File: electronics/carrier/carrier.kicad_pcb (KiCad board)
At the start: 2 copper layers, 100 x 70 mm, 15 parts, among them J1 5 V barrel input (fitted in r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, J2 USB-C power input, PD (laid o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, J3 S3 USB: link to the P4 and fl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, J4 5 V out to the P4 board's USB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, J5 HUB75 ribbon to the LED panel, J6 5 V power to the LED panel, J7 INMP441 microphone cable, J8 Future serial link to the P4'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, SW1 S3 reset, SW2 S3 boot, U1 ESP32-S3-WROOM-1-N16R8

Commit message: Add the carrier board schematic, generated from one netlist
tools/netlist.py describes every part and pin net; gen_schematic.py writes
the KiCad schematic from it and build_board.py puts every pad on its net, so
the schematic and board cannot disagree (KiCad parity check: 0 differences;
ERC clean apart from three intentional input ties).

Circuit: barrel 5 V input with polyfuse, TVS and bulk capacitance; USB-C PD
path laid out but not fitted (CH224A requesting 15 V, TPS568215 to 5 V with
TI's datasheet values) selected by solder jumper; AP2112K 3.3 V;
ESP32-S3-WROOM-1 with reset/boot, USB-C with ESD protection and 5.1k CC
resistors; two 74AHCT245 buffers to a standard HUB75 socket on the firmware's
existing GPIOs; microphone, fused P4 power and future UART connectors.

Co-Authored-By: Claude Opus 5.5 <noreply@anthropic.com>
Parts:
- added C1: 1000uF 10V, Capacitor_SMD:CP_Elec_10x10.5, F.Cu at (195.0, 82.0)
- added C10: 1uF 25V, Capacitor_SMD:C_0805_2012Metric, F.Cu at (217.0, 73.0)
- added C11: 100nF, Capacitor_SMD:C_0603_1608Metric, F.Cu at (217.0, 91.0)
- added C12: 150pF, Capacitor_SMD:C_0603_1608Metric, F.Cu at (217.0, 127.0)
- added C13: 4.7uF, Capacitor_SMD:C_0805_2012Metric, F.Cu at (217.0, 154.0)
- added C14: 10uF 25V, Capacitor_SMD:C_1206_3216Metric, F.Cu at (217.0, 181.0)
- added C15: 10uF 25V, Capacitor_SMD:C_1206_3216Metric, F.Cu at (217.0, 190.0)
- added C16: 10uF 25V, Capacitor_SMD:C_1206_3216Metric, F.Cu at (217.0, 199.0)
- added C17: 10uF 25V, Capacitor_SMD:C_1206_3216Metric, F.Cu at (217.0, 208.0)
- added C18: 100nF 25V, Capacitor_SMD:C_0603_1608Metric, F.Cu at (217.0, 217.0)
- added C19: 22uF 10V, Capacitor_SMD:C_1206_3216Metric, F.Cu at (217.0, 226.0)
- added C2: 22uF 10V, Capacitor_SMD:C_1206_3216Metric, F.Cu at (195.0, 91.0)
- added C20: 22uF 10V, Capacitor_SMD:C_1206_3216Metric, F.Cu at (217.0, 235.0)
- added C21: 22uF 10V, Capacitor_SMD:C_1206_3216Metric, F.Cu at (217.0, 244.0)
- added C22: 22uF 10V, Capacitor_SMD:C_1206_3216Metric, F.Cu at (217.0, 253.0)
- added C23: 22uF 10V, Capacitor_SMD:C_1206_3216Metric, F.Cu at (217.0, 262.0)
- added C24: 100nF, Capacitor_SMD:C_0603_1608Metric, F.Cu at (283.0, 82.0)
- added C25: 100nF, Capacitor_SMD:C_0603_1608Metric, F.Cu at (283.0, 91.0)
- added C3: 100nF, Capacitor_SMD:C_0603_1608Metric, F.Cu at (195.0, 100.0)
- added C4: 1uF, Capacitor_SMD:C_0603_1608Metric, F.Cu at (261.0, 64.0)
- added C5: 22uF, Capacitor_SMD:C_1206_3216Metric, F.Cu at (261.0, 82.0)
- added C6: 100nF, Capacitor_SMD:C_0603_1608Metric, F.Cu at (261.0, 91.0)
- added C7: 1uF, Capacitor_SMD:C_0603_1608Metric, F.Cu at (239.0, 64.0)
- added C8: 1uF, Capacitor_SMD:C_0603_1608Metric, F.Cu at (239.0, 73.0)
- added D1: SMAJ5.0A, Diode_SMD:D_SMA, F.Cu at (195.0, 73.0)
- added D2: Green, LED_SMD:LED_0603_1608Metric, F.Cu at (239.0, 82.0)
- added F1: 6A hold, Fuse:Fuse_2920_7451Metric, F.Cu at (195.0, 55.0)
- added F2: 2.5A hold, Fuse:Fuse_1812_4532Metric, F.Cu at (305.0, 55.0)
- added JP1: Barrel input, Jumper:SolderJumper-2_P1.3mm_Bridged_RoundedPad1.0x1.5mm, F.Cu at (195.0, 64.0)
- added JP2: USB-C input, Jumper:SolderJumper-2_P1.3mm_Open_RoundedPad1.0x1.5mm, F.Cu at (217.0, 271.0)
- added L1: 2.2uH 10A, Inductor_SMD:L_Coilcraft_XAL7070-XXX, F.Cu at (217.0, 100.0)
- added R1: 10k, Resistor_SMD:R_0603_1608Metric, F.Cu at (261.0, 55.0)
- added R10: 56k, Resistor_SMD:R_0603_1608Metric, F.Cu at (217.0, 64.0)
- added R11: 73.2k, Resistor_SMD:R_0603_1608Metric, F.Cu at (217.0, 109.0)
- added R12: 10k, Resistor_SMD:R_0603_1608Metric, F.Cu at (217.0, 118.0)
- added R13: 100k, Resistor_SMD:R_0603_1608Metric, F.Cu at (217.0, 136.0)
- added R14: 10k, Resistor_SMD:R_0603_1608Metric, F.Cu at (217.0, 145.0)
- added R15: 120k, Resistor_SMD:R_0603_1608Metric, F.Cu at (217.0, 163.0)
- added R16: 20k, Resistor_SMD:R_0603_1608Metric, F.Cu at (217.0, 172.0)
- added R2: 10k, Resistor_SMD:R_0603_1608Metric, F.Cu at (261.0, 73.0)
- added R3: 5.1k, Resistor_SMD:R_0603_1608Metric, F.Cu at (261.0, 100.0)
- added R4: 5.1k, Resistor_SMD:R_0603_1608Metric, F.Cu at (261.0, 109.0)
- added R5: 1k, Resistor_SMD:R_0603_1608Metric, F.Cu at (239.0, 91.0)
- added R6: 10k, Resistor_SMD:R_0603_1608Metric, F.Cu at (283.0, 55.0)
- added U2: CH224A, Package_SO:SSOP-10-1EP_3.9x4.9mm_P1mm_EP2.1x3.3mm, F.Cu at (217.0, 55.0)
- added U3: TPS568215, Package_DFN_QFN:Texas_RNN0018A, F.Cu at (217.0, 82.0)
- added U4: USBLC6-2SC6, Package_TO_SOT_SMD:SOT-23-6, F.Cu at (261.0, 118.0)
- added U5: AP2112K-3.3, Package_TO_SOT_SMD:SOT-23-5, F.Cu at (239.0, 55.0)
- added U6: 74AHCT245, Package_SO:TSSOP-20_4.4x6.5mm_P0.65mm, F.Cu at (283.0, 64.0)
- added U7: 74AHCT245, Package_SO:TSSOP-20_4.4x6.5mm_P0.65mm, F.Cu at (283.0, 73.0)
- H1, H2, H3, H4: value M3 to heat-set insert -> M3; footprint MountingHole_3.2mm_M3 -> MountingHole:MountingHole_3.2mm_M3
- J1: value 5 V barrel input (fitted in revision 1) -> PJ-063AH; footprint BarrelJack_CUI_PJ-063AH_Horizontal -> Connector_BarrelJack:BarrelJack_CUI_PJ-063AH_Horizontal
- J2: value USB-C power input, PD (laid out, fitted later) -> USB-C power in; footprint USB_C_Receptacle_HRO_TYPE-C-31-M-12 -> Connector_USB:USB_C_Receptacle_HRO_TYPE-C-31-M-12
- J3: value S3 USB: link to the P4 and flashing -> S3 USB (P4 link, flashing); footprint USB_C_Receptacle_GCT_USB4105-xx-A_16P_TopMnt_Horizontal -> Connector_USB:USB_C_Receptacle_GCT_USB4105-xx-A_16P_TopMnt_Horizontal
- J4: value 5 V out to the P4 board's USB-C -> 5V to P4; footprint USB_A_Molex_67643_Horizontal -> Connector_USB:USB_A_Molex_67643_Horizontal
- J5: value HUB75 ribbon to the LED panel -> HUB75; footprint IDC-Header_2x08_P2.54mm_Vertical -> Connector_IDC:IDC-Header_2x08_P2.54mm_Vertical
- J6: value 5 V power to the LED panel -> LED panel 5V; footprint TerminalBlock_Phoenix_MKDS-1,5-2-5.08_1x02_P5.08mm_Horizontal -> TerminalBlock_Phoenix:TerminalBlock_Phoenix_MKDS-1,5-2-5.08_1x02_P5.08mm_Horizontal
- J7: value INMP441 microphone cable -> INMP441; footprint JST_PH_B6B-PH-K_1x06_P2.00mm_Vertical -> Connector_JST:JST_PH_B6B-PH-K_1x06_P2.00mm_Vertical
- J8: value Future serial link to the P4's UART socket (not fitted) -> P4 UART (future); footprint JST_PH_B4B-PH-K_1x04_P2.00mm_Vertical -> Connector_JST:JST_PH_B4B-PH-K_1x04_P2.00mm_Vertical
- SW1: value S3 reset -> Reset; footprint SW_SPST_TL3342 -> Button_Switch_SMD:SW_SPST_TL3342
- SW2: value S3 boot -> Boot; footprint SW_SPST_TL3342 -> Button_Switch_SMD:SW_SPST_TL3342
- U1: footprint ESP32-S3-WROOM-1 -> RF_Module:ESP32-S3-WROOM-1
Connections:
- J1 pad 1: (no net) -> /VIN_BARREL
- J1 pad 2: (no net) -> /GND
- J2 pad A1: (no net) -> /GND
- J2 pad A12: (no net) -> /GND
- J2 pad A4: (no net) -> /VBUS_PD
- J2 pad A5: (no net) -> /PD_CC1
- J2 pad A6: (no net) -> unconnected-(J2-D+-PadA6)
- J2 pad A7: (no net) -> unconnected-(J2-D--PadA7)
- J2 pad A8: (no net) -> unconnected-(J2-SBU1-PadA8)
- J2 pad A9: (no net) -> /VBUS_PD
- J2 pad B1: (no net) -> /GND
- J2 pad B12: (no net) -> /GND
- J2 pad B4: (no net) -> /VBUS_PD
- J2 pad B5: (no net) -> /PD_CC2
- J2 pad B6: (no net) -> unconnected-(J2-D+-PadB6)
- J2 pad B7: (no net) -> unconnected-(J2-D--PadB7)
- J2 pad B8: (no net) -> unconnected-(J2-SBU2-PadB8)
- J2 pad B9: (no net) -> /VBUS_PD
- J2 pad SH: (no net) -> /GND
- J3 pad A1: (no net) -> /GND
- J3 pad A12: (no net) -> /GND
- J3 pad A4: (no net) -> /S3_VBUS
- J3 pad A5: (no net) -> /S3_CC1
- J3 pad A6: (no net) -> /USB_DP
- J3 pad A7: (no net) -> /USB_DM
- J3 pad A8: (no net) -> unconnected-(J3-SBU1-PadA8)
- J3 pad A9: (no net) -> /S3_VBUS
- J3 pad B1: (no net) -> /GND
- J3 pad B12: (no net) -> /GND
- J3 pad B4: (no net) -> /S3_VBUS
- J3 pad B5: (no net) -> /S3_CC2
- J3 pad B6: (no net) -> /USB_DP
- J3 pad B7: (no net) -> /USB_DM
- J3 pad B8: (no net) -> unconnected-(J3-SBU2-PadB8)
- J3 pad B9: (no net) -> /S3_VBUS
- J3 pad SH: (no net) -> /GND
- J4 pad 1: (no net) -> /P4_5V
- J4 pad 2: (no net) -> unconnected-(J4-D--Pad2)
- J4 pad 3: (no net) -> unconnected-(J4-D+-Pad3)
- J4 pad 4: (no net) -> /GND
- J4 pad SH: (no net) -> /GND
- J5 pad 1: (no net) -> /HUB_R1
- J5 pad 10: (no net) -> /HUB_B
- J5 pad 11: (no net) -> /HUB_C
- J5 pad 12: (no net) -> /HUB_D
- J5 pad 13: (no net) -> /HUB_CLK
- J5 pad 14: (no net) -> /HUB_LAT
- J5 pad 15: (no net) -> /HUB_OE
- J5 pad 16: (no net) -> /GND
- J5 pad 2: (no net) -> /HUB_G1
- J5 pad 3: (no net) -> /HUB_B1
- J5 pad 4: (no net) -> /GND
- J5 pad 5: (no net) -> /HUB_R2
- J5 pad 6: (no net) -> /HUB_G2
- J5 pad 7: (no net) -> /HUB_B2
- J5 pad 8: (no net) -> /GND
- J5 pad 9: (no net) -> /HUB_A
- J6 pad 1: (no net) -> /+5V
- J6 pad 2: (no net) -> /GND
- J7 pad 1: (no net) -> /+3V3
- J7 pad 2: (no net) -> /GND
- J7 pad 3: (no net) -> /MIC_SCK
- J7 pad 4: (no net) -> /MIC_WS
- J7 pad 5: (no net) -> /MIC_SD
- J7 pad 6: (no net) -> /GND
- J8 pad 1: (no net) -> /GND
- J8 pad 2: (no net) -> /S3_UART_TX
- J8 pad 3: (no net) -> /S3_UART_RX
- J8 pad 4: (no net) -> unconnected-(J8-Pin_4-Pad4)
- SW1 pad 1: (no net) -> /S3_EN
- SW1 pad 2: (no net) -> /GND
- SW2 pad 1: (no net) -> /S3_BOOT
- SW2 pad 2: (no net) -> /GND
- U1 pad 1: (no net) -> /GND
- U1 pad 10: (no net) -> /S3_CLK
- U1 pad 11: (no net) -> /S3_LAT
- U1 pad 12: (no net) -> /S3_G1
- U1 pad 13: (no net) -> /USB_DM
- U1 pad 14: (no net) -> /USB_DP
- U1 pad 15: (no net) -> unconnected-(U1-IO3-Pad15)
- U1 pad 16: (no net) -> unconnected-(U1-IO46-Pad16)
- U1 pad 17: (no net) -> /S3_B1
- U1 pad 18: (no net) -> /S3_R2
- U1 pad 19: (no net) -> /S3_G2
- U1 pad 2: (no net) -> /+3V3
- U1 pad 20: (no net) -> /S3_B2
- U1 pad 21: (no net) -> /S3_A
- U1 pad 22: (no net) -> /S3_B
- U1 pad 23: (no net) -> /S3_OE
- U1 pad 24: (no net) -> unconnected-(U1-IO47-Pad24)
- U1 pad 25: (no net) -> unconnected-(U1-IO48-Pad25)
- U1 pad 26: (no net) -> unconnected-(U1-IO45-Pad26)
- U1 pad 27: (no net) -> /S3_BOOT
- U1 pad 28: (no net) -> unconnected-(U1-IO35-Pad28)
- U1 pad 29: (no net) -> unconnected-(U1-IO36-Pad29)
- U1 pad 3: (no net) -> /S3_EN
- U1 pad 30: (no net) -> unconnected-(U1-IO37-Pad30)
- U1 pad 31: (no net) -> unconnected-(U1-IO38-Pad31)
- U1 pad 32: (no net) -> unconnected-(U1-IO39-Pad32)
- U1 pad 33: (no net) -> unconnected-(U1-IO40-Pad33)
- U1 pad 34: (no net) -> unconnected-(U1-IO41-Pad34)
- U1 pad 35: (no net) -> unconnected-(U1-IO42-Pad35)
- U1 pad 36: (no net) -> unconnected-(U1-RXD0-Pad36)
- U1 pad 37: (no net) -> unconnected-(U1-TXD0-Pad37)
- U1 pad 38: (no net) -> /S3_UART_RX
- U1 pad 39: (no net) -> /S3_UART_TX
- U1 pad 4: (no net) -> /S3_R1
- U1 pad 40: (no net) -> /GND
- U1 pad 41: (no net) -> /GND
- U1 pad 5: (no net) -> /MIC_SCK
- U1 pad 6: (no net) -> /MIC_WS
- U1 pad 7: (no net) -> /MIC_SD
- U1 pad 8: (no net) -> /S3_C
- U1 pad 9: (no net) -> /S3_D

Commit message: Place every carrier board part
Power-input protection under the barrel socket; the USB-C power section
grouped at the rear middle by its socket; the 3.3 V supply and decoupling
beside the module; ESD and CC resistors at the S3's USB-C; the buffers
between the module and the HUB75 socket; buttons and the power LED on the
front strip. Nothing in the module's antenna keep-out; schematic parity 0.

Co-Authored-By: Claude Opus 5.5 <noreply@anthropic.com>
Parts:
- moved F2 238.2 mm to (70.0, 94.0), turned to 90 degrees
- moved JP2 215.3 mm to (118.5, 79.5)
- moved C23 211.1 mm to (118.0, 75.5)
- moved C22 203.6 mm to (113.0, 78.0)
- moved U4 201.9 mm to (64.0, 74.0), turned to 90 degrees
- moved R3 201.3 mm to (62.0, 69.5)
- moved R4 201.2 mm to (62.0, 79.0)
- moved C21 198.0 mm to (113.0, 75.5)
- moved C20 191.1 mm to (108.0, 78.0)
- moved U6 190.7 mm to (94.0, 89.5), turned to 90 degrees
- moved C24 189.0 mm to (94.0, 83.5)
- moved C18 186.0 mm to (100.5, 72.0), turned to 90 degrees
- moved C19 185.8 mm to (108.0, 75.5)
- moved C17 185.0 mm to (91.0, 72.5), turned to 90 degrees
- moved R2 181.7 mm to (83.5, 112.0), turned to 90 degrees
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
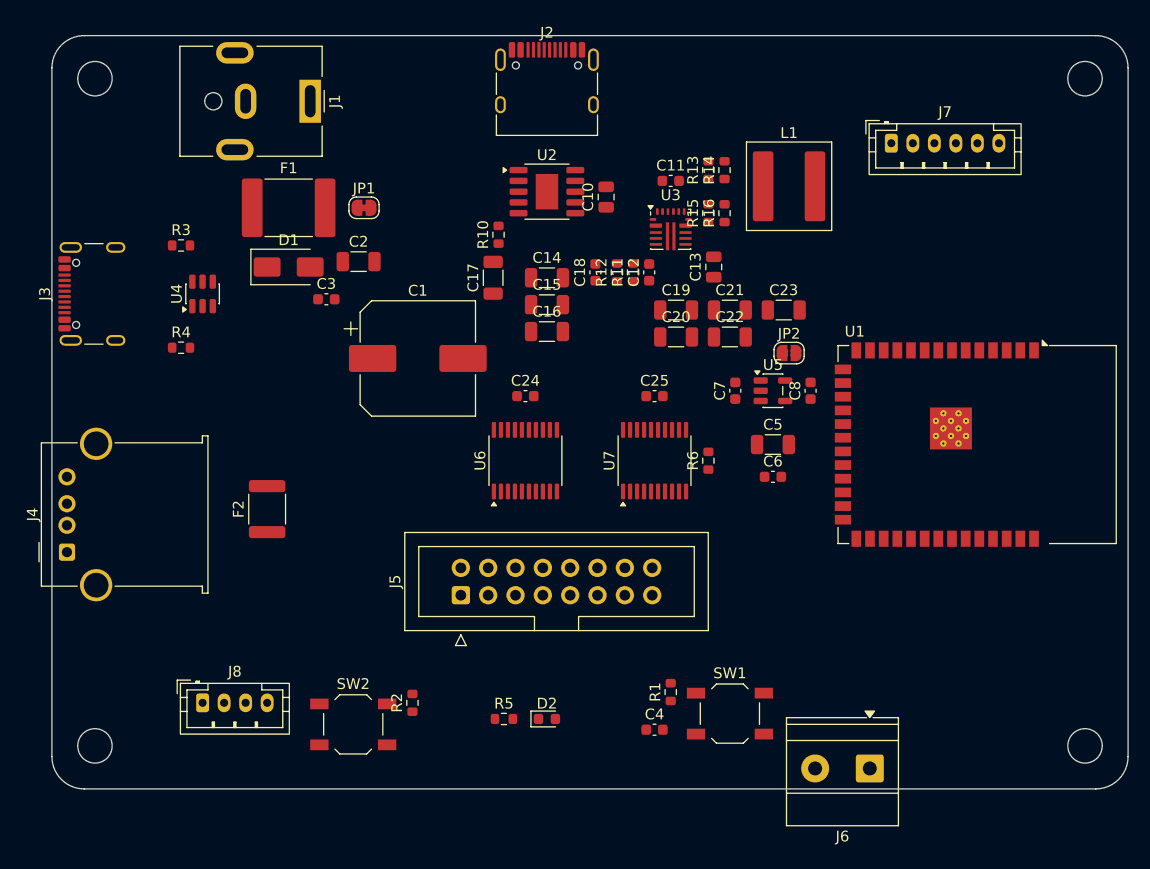
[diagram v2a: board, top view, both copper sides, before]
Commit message: Route the carrier board
Add route_board.py: locked high-current and fine-pitch copper, Freerouting
for the rest, ground pours and stitching vias, then KiCad's own check for
anything left unconnected. The board passes DRC with no errors, nothing
unconnected and exact schematic parity.

- Remove the solder jumpers: F1 alone selects the barrel input, and the
  USB-C buck output feeds +5V directly.
- Name stacked unconnected pins as KiCad does, so the S3 socket's paired
  VBUS pads share one net.
- Rotate U3 so its switch node runs straight to L1; move the MODE/EN
  dividers and the boot capacitor to suit. Swap R3/R4 to match their CC pins.
- Hide chip passive references on the silkscreen; allow ref positions in
  board.json; allow one thermal spoke on through-hole pads (.kicad_dru).

Co-Authored-By: Claude Opus 5.5 <noreply@anthropic.com>
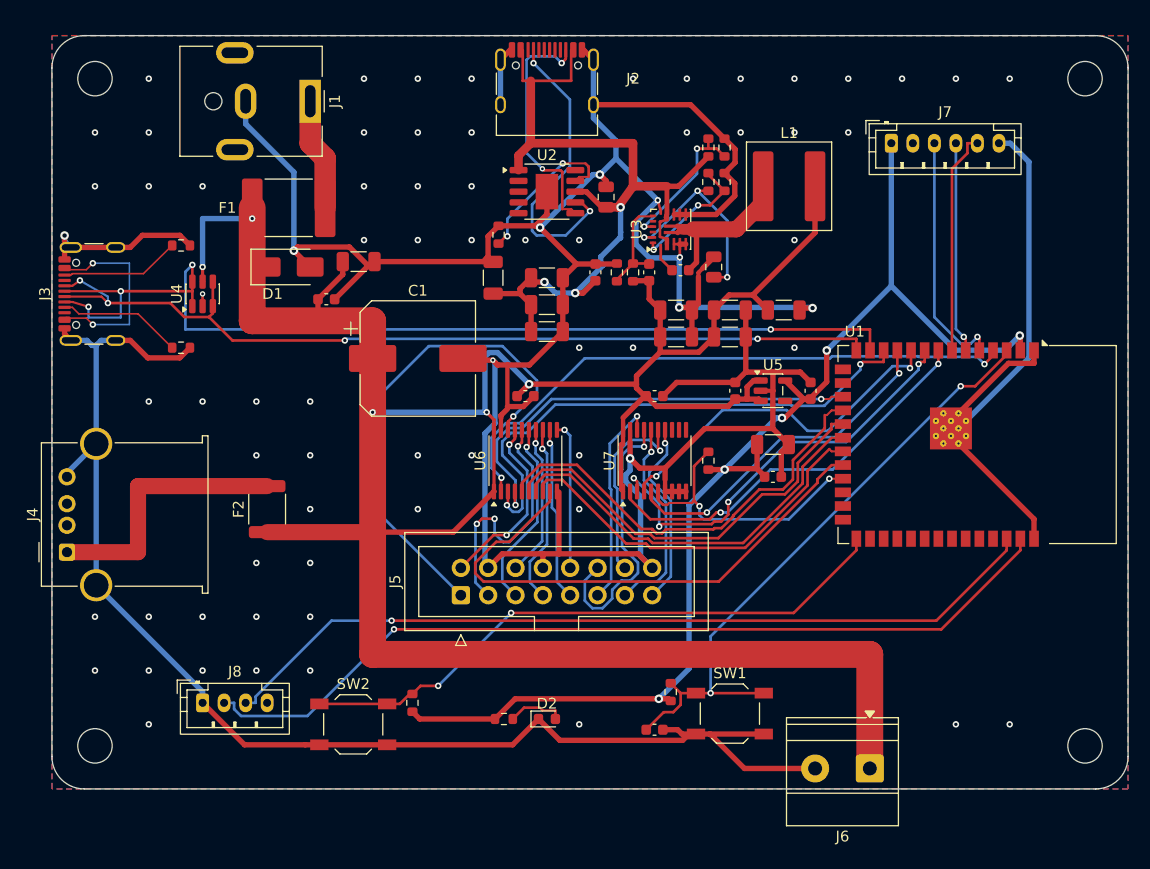
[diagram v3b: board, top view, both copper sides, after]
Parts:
- removed JP1: Barrel input, Jumper:SolderJumper-2_P1.3mm_Bridged_RoundedPad1.0x1.5mm
- removed JP2: USB-C input, Jumper:SolderJumper-2_P1.3mm_Open_RoundedPad1.0x1.5mm
- moved R3 9.50 mm to (62.0, 79.0)
- moved R4 9.50 mm to (62.0, 69.5)
- moved C11 8.35 mm to (108.4, 71.8)
- moved R15 2.90 mm to (111.0, 63.6)
- moved R16 2.90 mm to (112.5, 63.6)
- moved R13 2.10 mm to (111.0, 60.4)
- moved R14 2.10 mm to (112.5, 60.4)
- turned F1 to 180 degrees
- turned U3 to 90 degrees
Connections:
- C12 pad 1: /BUCK_OUT -> /+5V
- C19 pad 1: /BUCK_OUT -> /+5V
- C20 pad 1: /BUCK_OUT -> /+5V
- C21 pad 1: /BUCK_OUT -> /+5V
- C22 pad 1: /BUCK_OUT -> /+5V
- C23 pad 1: /BUCK_OUT -> /+5V
- F1 pad 2: /VIN_FUSED -> /+5V
- J3 pad A4: /S3_VBUS -> unconnected-(J3-VBUS-PadA4)
- J3 pad A9: /S3_VBUS -> unconnected-(J3-VBUS-PadA4)
- J3 pad B4: /S3_VBUS -> unconnected-(J3-VBUS-PadA4)
- J3 pad B9: /S3_VBUS -> unconnected-(J3-VBUS-PadA4)
- L1 pad 2: /BUCK_OUT -> /+5V
- R11 pad 1: /BUCK_OUT -> /+5V
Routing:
- net /GND: track 0.00 -> 503.3 mm, vias 0 -> 75
- net /+5V: track 0.00 -> 254.8 mm, vias 0 -> 5
- net /+3V3: track 0.00 -> 113.2 mm, vias 0 -> 5
- net /USB_DM: track 0.00 -> 96.3 mm, vias 0 -> 4
- net /USB_DP: track 0.00 -> 85.0 mm, vias 0 -> 4
- net /S3_UART_TX: track 0.00 -> 82.3 mm, vias 0 -> 1
- net /VBUS_PD: track 0.00 -> 79.6 mm, vias 0 -> 3
- net /S3_UART_RX: track 0.00 -> 78.0 mm, vias 0 -> 1
- net /S3_EN: track 0.00 -> 58.3 mm, vias 0 -> 2
- net /S3_BOOT: track 0.00 -> 56.9 mm, vias 0 -> 2
- net /S3_R1: track 0.00 -> 56.2 mm, vias 0 -> 2
- net /S3_B: track 0.00 -> 50.4 mm
- net /S3_G1: track 0.00 -> 50.1 mm, vias 0 -> 2
- net /HUB_R1: track 0.00 -> 46.3 mm, vias 0 -> 1
- net /S3_B1: track 0.00 -> 41.9 mm, vias 0 -> 2
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- added copper zone on B.Cu, net /GND
- added copper zone on F.Cu, net /GND

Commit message: Use a latching JST GH socket for the microphone
The PH socket held by friction only. Hand-draw the R13 sense link the
autorouter sometimes misses, and drop stitching vias that land on
isolated pour islands.

Co-Authored-By: Claude Opus 5.5 <noreply@anthropic.com>
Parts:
- J7: footprint Connector_JST:JST_PH_B6B-PH-K_1x06_P2.00mm_Vertical -> Connector_JST:JST_GH_BM06B-GHS-TBT_1x06-1MP_P1.25mm_Vertical
- moved J7 5.00 mm to (133.0, 60.0)
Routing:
- net /GND: track 503.3 -> 462.4 mm, vias 75 -> 72
- net /HUB_R1: track 46.3 -> 18.2 mm
- net /HUB_G2: track 14.1 -> 36.2 mm
- net /+5V: track 254.8 -> 273.6 mm, vias 5 -> 9
- net /HUB_C: track 19.5 -> 35.1 mm
- net /S3_B: track 50.4 -> 36.3 mm
- net /HUB_D: track 26.3 -> 14.6 mm
- net /HUB_LAT: track 18.1 -> 28.9 mm
- net /PD_CC1: track 27.9 -> 18.3 mm
- net /S3_OE: track 26.2 -> 34.5 mm, vias 2 -> 4
- net /S3_G1: track 50.1 -> 42.5 mm
- net /S3_B1: track 41.9 -> 34.9 mm
- net /S3_R2: track 40.5 -> 35.2 mm, vias 0 -> 2
- net /HUB_B2: track 16.7 -> 21.3 mm
- net /S3_G2: track 38.8 -> 34.2 mm, vias 0 -> 2
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
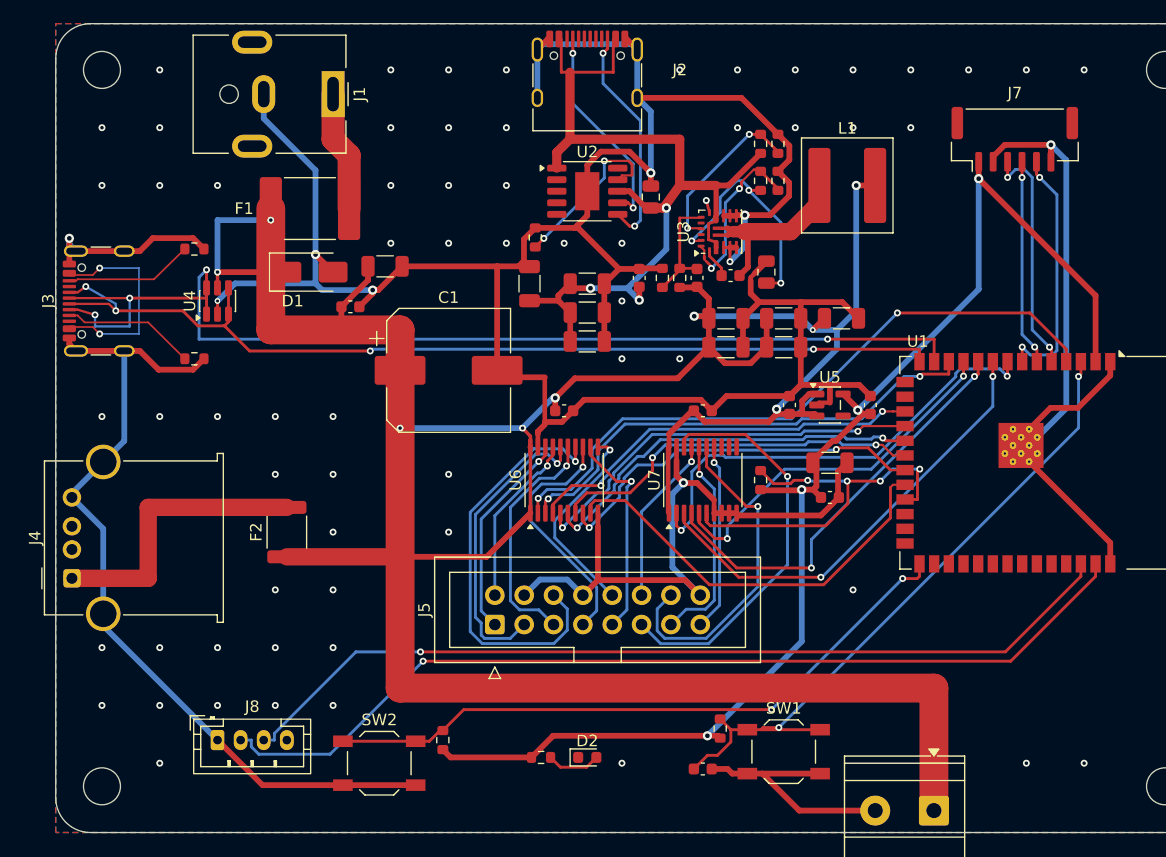
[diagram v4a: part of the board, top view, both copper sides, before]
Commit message: Use only standard 0.3 mm drills, for JLCPCB's base price
The small 0.25 mm vias and the S3 module's 0.2 mm ground-pad holes put
the board in a dearer via class. Also: hand-draw the C2 5 V link, ground
U7's OE patch with a via, and drill 0.3 mm any 0.5 mm via Freerouting
gives a supply net.

Co-Authored-By: Claude Opus 5.5 <noreply@anthropic.com>
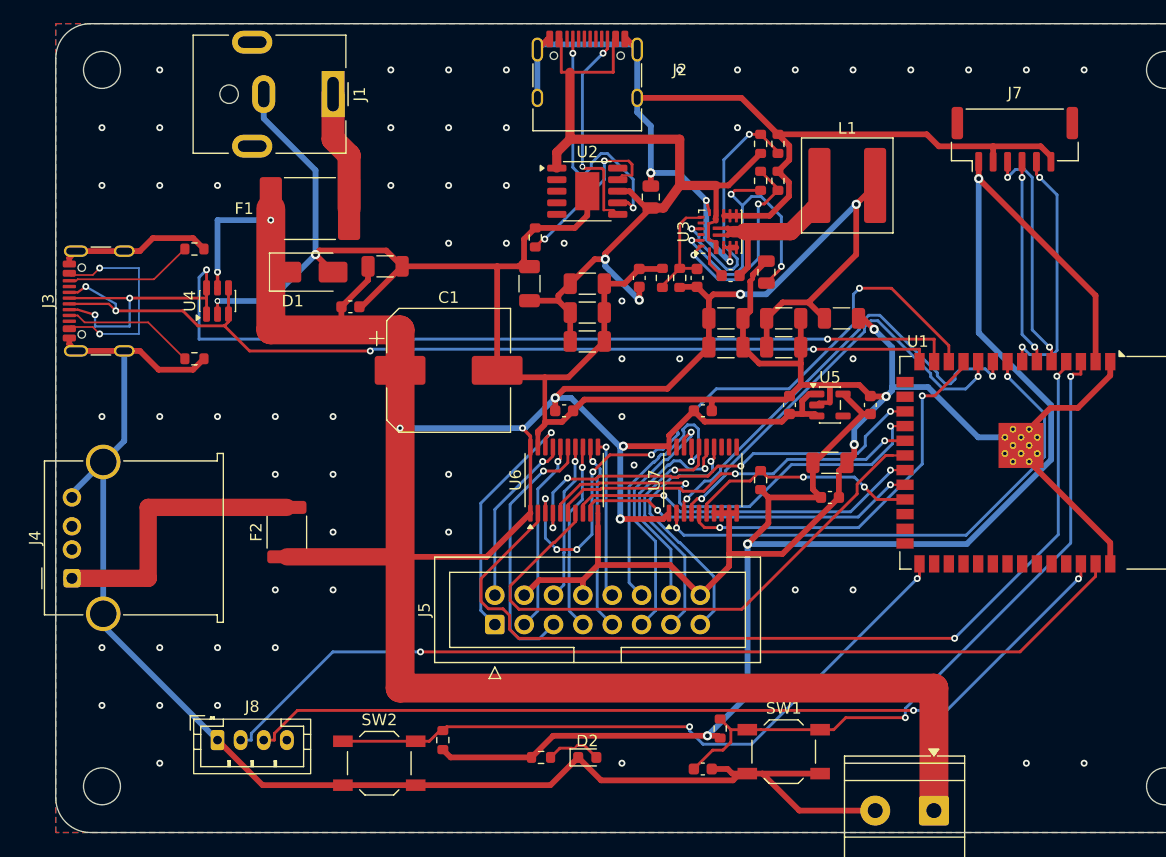
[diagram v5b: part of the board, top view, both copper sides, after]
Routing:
- net /GND: track 462.4 -> 499.4 mm, vias 72 -> 66
- net /+3V3: track 113.2 -> 143.6 mm, vias 4 -> 3
- net /S3_R1: track 57.0 -> 80.7 mm
- net /HUB_G2: track 36.2 -> 13.6 mm
- net /S3_B2: track 32.7 -> 50.4 mm, vias 2 -> 0
- net /S3_G1: track 42.5 -> 57.9 mm, vias 2 -> 6
- net /S3_OE: track 34.5 -> 20.2 mm, vias 4 -> 2
- net /HUB_C: track 35.1 -> 21.7 mm
- net /HUB_LAT: track 28.9 -> 19.1 mm
- net /HUB_B1: track 26.1 -> 16.7 mm
- net /HUB_D: track 14.6 -> 23.1 mm
- net /BUCK_EN: track 14.8 -> 22.6 mm
- net /S3_B: track 36.3 -> 29.8 mm, vias 0 -> 2
- net /BUCK_VREG5: track 20.6 -> 26.9 mm
- net /HUB_OE: track 16.3 -> 22.4 mm
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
